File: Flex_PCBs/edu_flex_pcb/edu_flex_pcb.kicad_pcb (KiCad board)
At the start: 2 copper layers, 11.4 x 68 mm, 2 parts, among them J1 Conn_01x22_Male, J2 Conn_01x22_Male

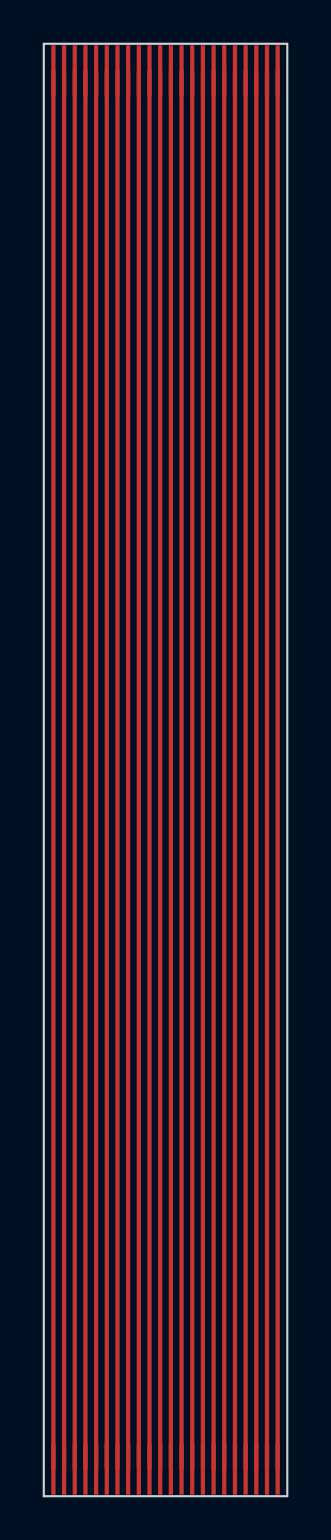
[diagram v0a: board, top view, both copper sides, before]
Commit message: Added small modifications to the existing flex PCBs plus the new ones: Y- and X-.
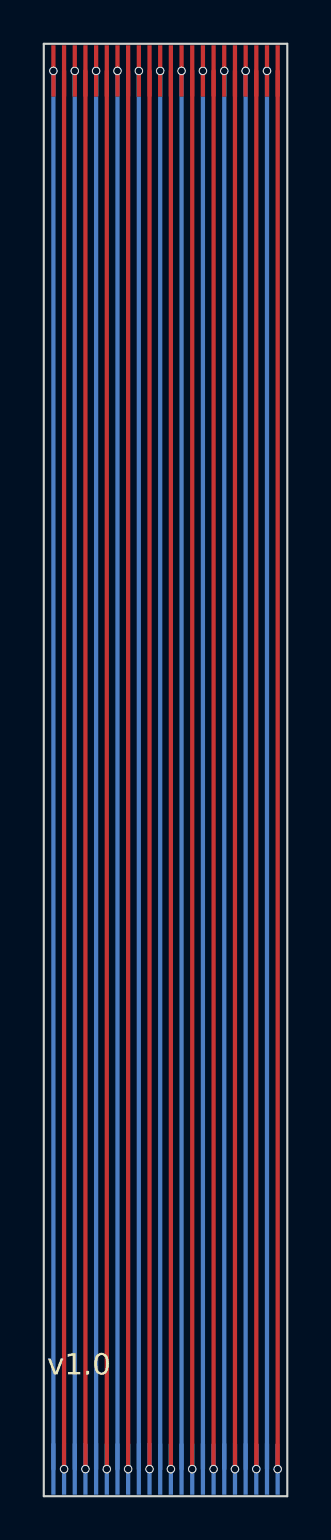
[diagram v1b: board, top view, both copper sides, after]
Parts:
- J2: moved to B.Cu
- moved J2 11.4 mm to (130.0, 129.4), turned to 0 degrees
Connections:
- J2 pad 1: 22 -> 1
- J2 pad 10: 13 -> 10
- J2 pad 11: 12 -> 11
- J2 pad 12: 11 -> 12
- J2 pad 13: 10 -> 13
- J2 pad 14: 9 -> 14
- J2 pad 15: 8 -> 15
- J2 pad 16: 7 -> 16
- J2 pad 17: 6 -> 17
- J2 pad 18: 5 -> 18
- J2 pad 19: 4 -> 19
- J2 pad 2: 21 -> 2
- J2 pad 20: 3 -> 20
- J2 pad 21: 2 -> 21
- J2 pad 22: 1 -> 22
- J2 pad 3: 20 -> 3
- J2 pad 4: 19 -> 4
- J2 pad 5: 18 -> 5
- J2 pad 6: 17 -> 6
- J2 pad 7: 16 -> 7
- J2 pad 8: 15 -> 8
- J2 pad 9: 14 -> 9
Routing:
- net 9: vias 0 -> 1
- net 8: vias 0 -> 1
- net 7: vias 0 -> 1
- net 6: vias 0 -> 1
- net 5: vias 0 -> 1
- net 4: vias 0 -> 1
- net 3: vias 0 -> 1
- net 22: vias 0 -> 1
- net 21: vias 0 -> 1
- net 20: vias 0 -> 1
- net 2: vias 0 -> 1
- net 19: vias 0 -> 1
- net 18: vias 0 -> 1
- net 17: vias 0 -> 1
- net 16: vias 0 -> 1
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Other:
- board text added: "The PCB should have a thickness of 0.12 mm (two Layer). On the marked areas in User.1 layer a 0.225 mm polyimide stiffener should be glued. The resulting gold fingers should have 0.3 mm in thickness."
- board text added: "v1.0"
- board text removed: "The PCB should have a thickness of 0.11 mm (one Layer). On the marked areas in User.1 layer a 0.25 mm polyimide stiffener should be glued. The resulting gold fingers should have 0.3 mm in thickness."
